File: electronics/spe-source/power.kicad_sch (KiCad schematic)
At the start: 21 parts, among them P2 CONN_01X02, U2 INA186A3, U5 AP2112K-3.3, U8 TPS26625

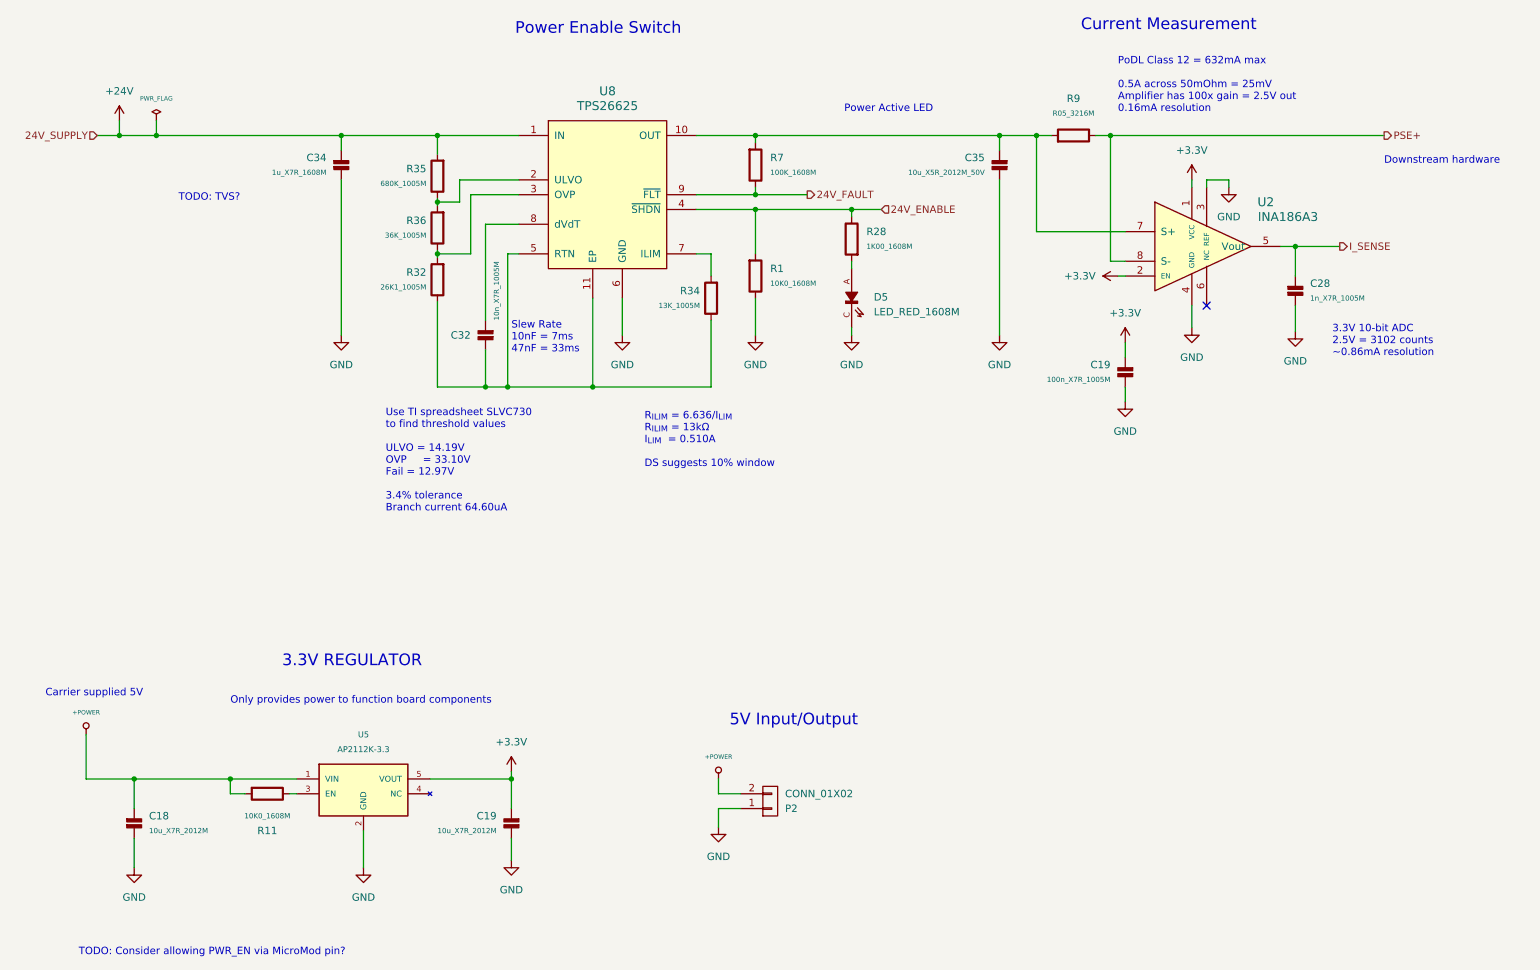
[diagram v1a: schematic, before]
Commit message: Revised PSE input voltage limit resistor values
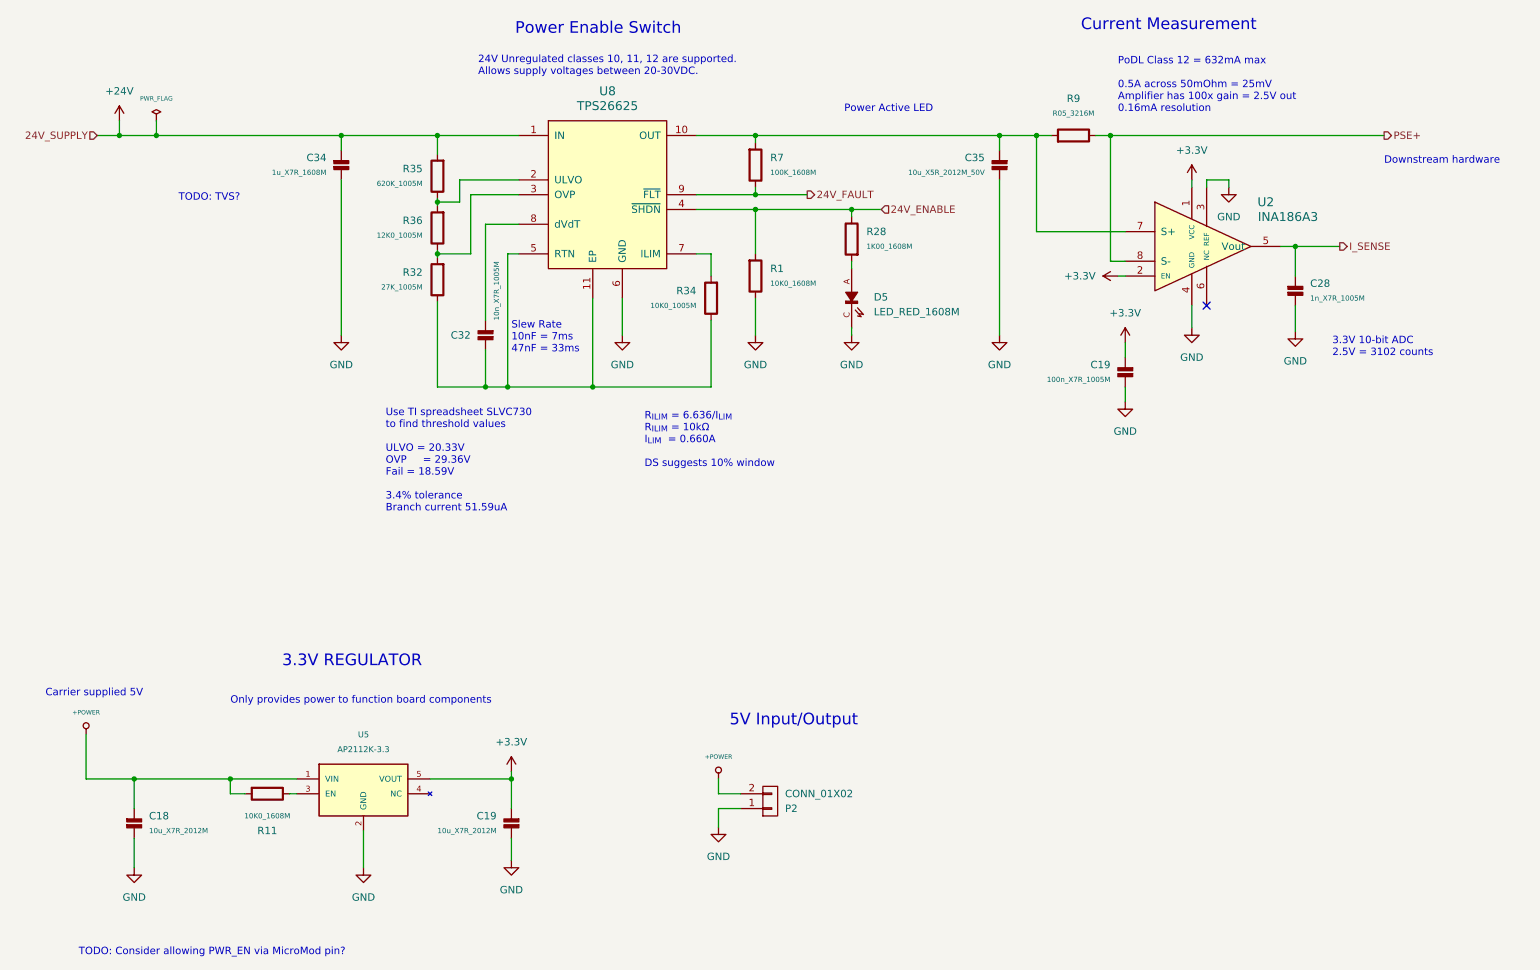
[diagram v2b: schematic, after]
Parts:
- removed R32: 26K1_1005M, Applidyne_Resistor:RESC1005X40N, symbol appli_resistor:26K1_1005M
- removed R34: 13K_1005M, Applidyne_Resistor:RESC1005X40N, symbol appli_resistor:13K_1005M
- removed R35: 680K_1005M, Applidyne_Resistor:RESC1005X40N, symbol appli_resistor:680K_1005M
- removed R36: 36K_1005M, Applidyne_Resistor:RESC1005X40N, symbol appli_resistor:36K_1005M
- added R32: 27K_1005M, Applidyne_Resistor:RESC1005X40N, symbol appli_resistor:27K_1005M
- added R34: 10K0_1005M, Applidyne_Resistor:RESC1005X40N, symbol appli_resistor:10K0_1005M
- added R35: 620K_1005M, Applidyne_Resistor:RESC1005X40N, symbol appli_resistor:620K_1005M
- added R36: 12K0_1005M, Applidyne_Resistor:RESC1005X40N, symbol appli_resistor:12K0_1005M
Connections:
- net +24V: now also R35.1
- net at U8.3 (OVP): now also R32.1, R36.2
- net at C32.2, U8.11 (EP), U8.5 (RTN): now also R32.2, R34.2
- net at U8.2 (ULVO): now also R35.2, R36.1
- net at U8.7 (ILIM): now also R34.1
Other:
- note added: "24V Unregulated classes 10, 11, 12 are supported. Allows supply voltages between 20-30VDC."
- note added: "3.3V 10-bit ADC 2.5V = 3102 counts"
- note added: "R_{ILIM} = 6.636/I_{LIM} R_{ILIM} = 10kΩ I_{LIM} = 0.660A DS suggests 10% window"
- note added: "Use TI spreadsheet SLVC730 to find threshold values ULVO = 20.33V OVP = 29.36V Fail = 18.59V 3.4% tolerance Branch current 51.59uA"
- note removed: "3.3V 10-bit ADC 2.5V = 3102 counts ~0.86mA resolution"
- note removed: "R_{ILIM} = 6.636/I_{LIM} R_{ILIM} = 13kΩ I_{LIM} = 0.510A DS suggests 10% window"
- note removed: "Use TI spreadsheet SLVC730 to find threshold values ULVO = 14.19V OVP = 33.10V Fail = 12.97V 3.4% tolerance Branch current 64.60uA"

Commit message: Minor tweaks to test sketches
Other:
- note added: "3.3V 12-bit ADC 2.5V = 3102 counts"
- note removed: "3.3V 10-bit ADC 2.5V = 3102 counts"
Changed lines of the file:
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@@
     (stroke (width 0) (type default))
   )
-  (text "3.3V 10-bit ADC\n2.5V = 3102 counts\n" (at 247.65 76.2 0)
+  (text "3.3V 12-bit ADC\n2.5V = 3102 counts\n" (at 247.65 76.2 0)
     (effects (font (size 1.27 1.27)) (justify left bottom))
   )
